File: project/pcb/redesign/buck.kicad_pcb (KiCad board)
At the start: 2 copper layers, 105.5 x 81 mm, 57 parts, among them J1 12V FUSED INPUT, J2 LOAD + / -, J3 NUCLEO-L432KC EXT USB, Q1 IRFZ44N TO-220, Q2 MMBT3904, U1 IR2110STRPBF, U2 78M05, U3 SN74HCT14DR, U4 SN74HCT00DR, U5 LM393BIDR, U6 INA180A1IDBVR

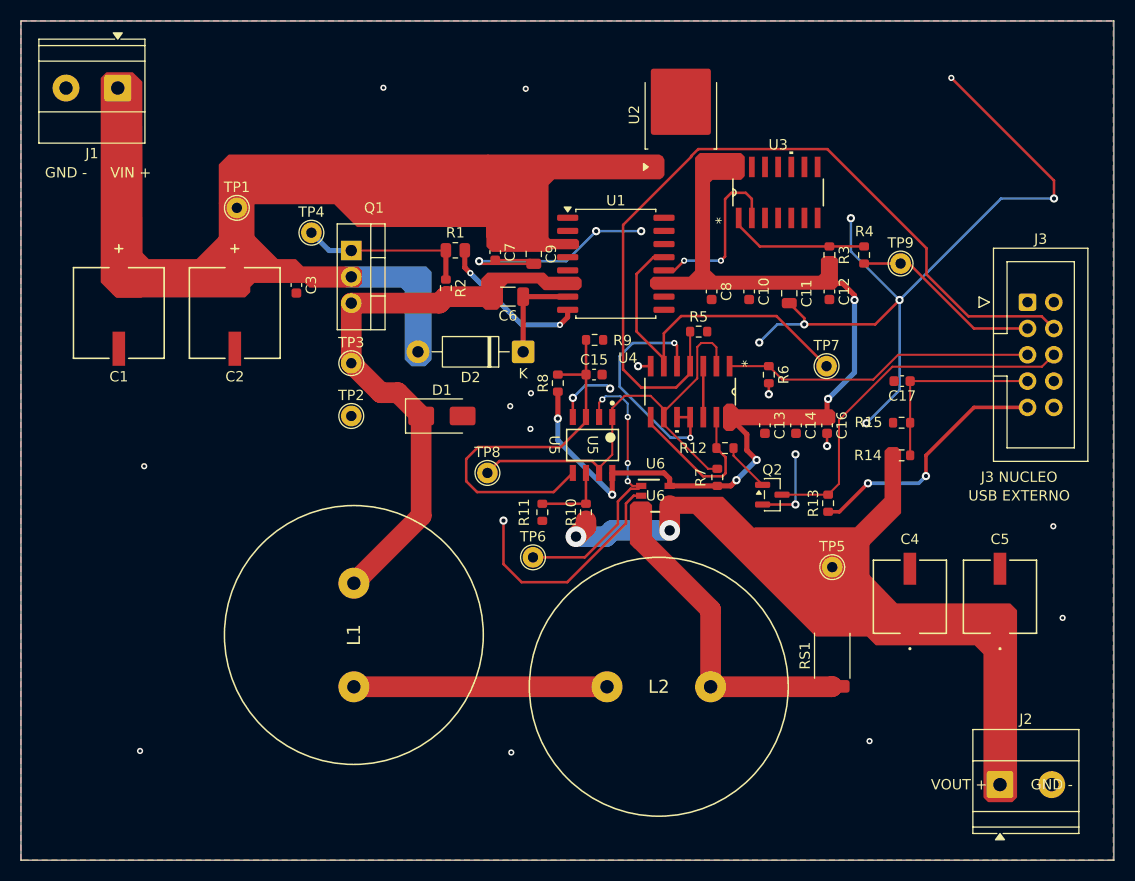
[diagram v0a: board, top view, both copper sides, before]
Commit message: feat: Buck PCB Rev B prototype package for JLCPCB
Rev B of project/pcb/redesign, prepared for a JLCPCB top-side SMT quote
and still pending bring-up. Rev A is preserved in history/revA_quote_20261027.

- Lands taken from manufacturer drawings (Murata 6000B, Same Sky TB002,
  Wurth WR-BHD, Panasonic SVPF/SVF, TA-I RLP, TI PW/DBV/DBZ/D/DBV5, Diodes
  SOD323); Q1 hole 1.4 mm per IPC-2222; U5 courtyard added.
- Power-domain interface: SN74LV4T125 buffer for PWM/RUN/RESET from +5V,
  TMUX1511 on the ADC path, TPS3808G33 supervisor, LM4040 2.5 V reference
  with BAT54WS clamps, fault latch set while the interface is disabled.
- Re-laid board: compact switching cell, no vias on HO/GATE/BOOT/SW,
  Kelvin sensing from RS1 inner edges, GND pours on both layers.
- L432KC firmware: Rev B ADC scale (6.4844 mV/count), VOUT-collapse fault,
  host test.
- Fabrication package production/jlcpcb-revB-2026-10-27: DRC 0 errors,
  0 unconnected, 0 parity; ERC 0 errors.

Not ready to order: L1/L2 have no JLC/LCSC stock, the LM4040 X-variant and
R10 supply need decisions, the JLC viewer rotation check and ARM build are
pending. BUCK_BOARD_REVIEWED stays 0. See revB_release_report.md.

Co-Authored-By: Claude Opus 5.5 <noreply@anthropic.com>
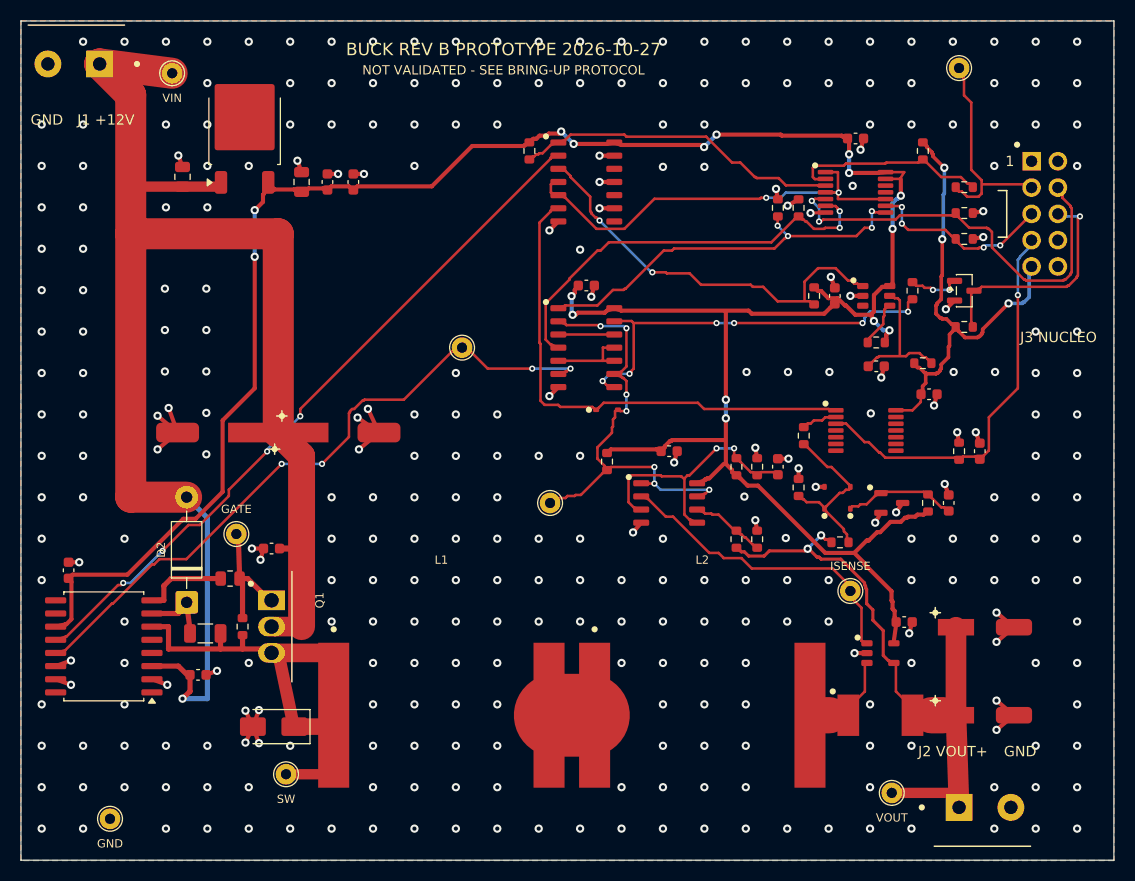
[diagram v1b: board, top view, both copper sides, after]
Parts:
- added C18: 100nF, Capacitor_SMD:C_0603_1608Metric, F.Cu at (186.0, 42.8)
- added C19: 100nF, Capacitor_SMD:C_0603_1608Metric, F.Cu at (193.1, 67.5)
- added C20: 100nF, Capacitor_SMD:C_0603_1608Metric, F.Cu at (184.0, 58.0)
- added C21: 1nF, Capacitor_SMD:C_0603_1608Metric, F.Cu at (188.0, 64.8)
- added C22: 100nF, Capacitor_SMD:C_0603_1608Metric, F.Cu at (195.0, 78.0)
- added D3: BAT54WS-7-F, Buck_RevB:Diodes_SOD323, F.Cu at (183.0, 77.5)
- added D4: BAT54WS-7-F, Buck_RevB:Diodes_SOD323, F.Cu at (185.5, 77.5)
- added D5: BAT54WS-7-F, Buck_RevB:Diodes_SOD323, F.Cu at (162.0, 69.0)
- added R16: 10k, Resistor_SMD:R_0603_1608Metric, F.Cu at (180.5, 49.5)
- added R17: 10k, Resistor_SMD:R_0603_1608Metric, F.Cu at (178.5, 49.5)
- added R18: 100k, Resistor_SMD:R_0603_1608Metric, F.Cu at (192.5, 44.0)
- added R19: 22k, Resistor_SMD:R_0603_1608Metric, F.Cu at (182.0, 58.0)
- added R20: 1k 1%, Resistor_SMD:R_0603_1608Metric, F.Cu at (181.0, 71.5)
- added R21: 100k 1%, Resistor_SMD:R_0603_1608Metric, F.Cu at (196.0, 73.0)
- added R22: 10k, Resistor_SMD:R_0603_1608Metric, F.Cu at (192.5, 64.5)
- added R23: 2.2k, Resistor_SMD:R_0603_1608Metric, F.Cu at (193.0, 78.0)
- added R24: 100k, Resistor_SMD:R_0603_1608Metric, F.Cu at (188.0, 62.5)
- added U10: LM4040AIM3X-2.5/NOPB, Buck_RevB:TI_DBZ0003A_SOT-23-3, F.Cu at (189.5, 78.0)
- added U7: SN74LV4T125PWR, Buck_RevB:TI_PW0014A_TSSOP-14, F.Cu at (186.0, 48.0)
- added U8: TMUX1511PWR, Buck_RevB:TI_PW0014A_TSSOP-14, F.Cu at (187.0, 71.0)
- added U9: TPS3808G33DBVR, Buck_RevB:TI_DBV0006A_SOT-23-6, F.Cu at (188.0, 58.0)
- C1, C2: footprint Buck_SMD:PCAP_SVP_E7_PAN -> Buck_RevB:CP_Panasonic_SVPF_E7_Land
- C4, C5: value 10uF 35V low ESR -> 10uF 50V 50SVF10M; footprint Buck_SMD:CAP_SVF_C6_PAN -> Buck_RevB:CP_Panasonic_SVF_C6_Land
- D2: value UF4004 -> UF4004-E3/54
- J1: value 12V FUSED INPUT -> 12V IN TB002-500-02BE; footprint TerminalBlock_Phoenix:TerminalBlock_Phoenix_MKDS-1,5-2_1x02_P5.00mm_Horizontal -> Buck_RevB:TerminalBlock_SameSky_TB002-500-02_1x02_P5.00mm
- J2: value LOAD + / - -> LOAD TB002-500-02BE; footprint TerminalBlock_Phoenix:TerminalBlock_Phoenix_MKDS-1,5-2_1x02_P5.00mm_Horizontal -> Buck_RevB:TerminalBlock_SameSky_TB002-500-02_1x02_P5.00mm
- J3: value NUCLEO-L432KC EXT USB -> NUCLEO IF 61201021621; footprint Connector_IDC:IDC-Header_2x05_P2.54mm_Vertical -> Buck_RevB:Wurth_WR-BHD_61201021621_2x05_P2.54mm_Vertical
- L1, L2: value 330uH >=3A Isat VERIFY -> 330uH 60B334C; footprint Buck:Inductor_25mm_P10mm_VERIFY -> Buck_RevB:L_Murata_6000B_27.0x23.5mm
- Q1: value IRFZ44N TO-220 -> IRFZ44NPBF; footprint Package_TO_SOT_THT:TO-220-3_Vertical -> Buck_RevB:TO-220-3_Vertical_Drill1.4
- RS1: value 0.050R 1% 1W -> 0.050R 1% 2W RLP25FEER050; footprint Resistor_SMD:R_2512_6332Metric -> Buck_RevB:R_TAI_RLP25_2512_Kelvin
- U3, U4: footprint Buck_SMD:D14 -> Buck_RevB:TI_D0014A_SOIC-14
- U5: footprint Buck_SMD:D0008A-MFG -> Buck_RevB:TI_D0008A_SOIC-8
- U6: footprint Buck_SMD:DBV0005A_N -> Buck_RevB:TI_DBV0005A_SOT-23-5
- moved C8 67.7 mm to (110.0, 84.5), turned to 90 degrees
- moved U1 61.7 mm to (113.4, 91.8), turned to 180 degrees
- moved C7 49.9 mm to (122.5, 94.6), turned to 0 degrees
- moved C11 48.3 mm to (132.5, 47.0), turned to 90 degrees
- moved C12 47.2 mm to (137.5, 47.0), turned to 90 degrees
- moved TP2 45.3 mm to (114.0, 108.5)
- moved C6 43.7 mm to (123.2, 90.6), turned to 0 degrees
- moved U2 42.2 mm to (127.0, 42.0)
- moved C10 42.1 mm to (135.0, 47.0), turned to 90 degrees
- moved D2 40.5 mm to (121.4, 87.6), turned to 90 degrees
- moved TP3 40.2 mm to (131.0, 104.2)
- moved R1 38.4 mm to (125.6, 85.3), turned to 0 degrees
- moved R2 38.1 mm to (126.8, 89.9)
- moved TP7 35.2 mm to (148.0, 63.0)
- moved C9 34.7 mm to (121.0, 46.5), turned to 90 degrees
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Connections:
- R14 pad 2: VSENSE -> VSENSE_DIV
- R15 pad 1: VSENSE -> VSENSE_DIV
- R4 pad 2: DPRIME -> PWM_IN
- U3 pad 3: GND -> NUC_PG
- U3 pad 4: unconnected-(U3-2Y-Pad4) -> BUF_OE_N
- U3 pad 5: GND -> BUF_OE_N
- U3 pad 6: unconnected-(U3-3Y-Pad6) -> ADC_EN
- U4 pad 1: RESET -> RESET_5V
- U4 pad 4: RUN -> RUN_5V
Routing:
- net +5V: track 53.1 -> 244.4 mm, vias 6 -> 16
- net VIN: track 0.00 -> 149.6 mm, vias 0 -> 1
- net GND: track 142.2 -> 79.9 mm, vias 29 -> 321
- net HIN: track 16.9 -> 68.7 mm, vias 2 -> 4
- net ADC_EN: track 0.00 -> 49.0 mm
- net RUN_5V: track 0.00 -> 40.7 mm, vias 0 -> 2
- net BUF_OE_N: track 0.00 -> 40.5 mm, vias 0 -> 2
- net VOUT: track 13.6 -> 53.8 mm
- net NUC_PG: track 0.00 -> 39.6 mm, vias 0 -> 2
- net RESET_5V: track 0.00 -> 38.4 mm, vias 0 -> 4
- net RUN: track 79.1 -> 41.1 mm, vias 0 -> 2
- net SD: track 34.9 -> 65.3 mm, vias 0 -> 4
- net IP: track 28.7 -> 4.53 mm
- net FAULT: track 15.9 -> 39.7 mm, vias 0 -> 6
- net LMID: track 24.4 -> 3.20 mm
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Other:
- board text added: "1"
- board text added: "BUCK REV B PROTOTYPE 2026-10-27"
- board text added: "GATE"
- board text added: "GND"
- board text added: "ISENSE"
- board text added: "J1 +12V"
- board text added: "J2 VOUT+"
- board text added: "NOT VALIDATED - SEE BRING-UP PROTOCOL"
- board text added: "SW"
- board text added: "VIN"
- board text added: "VOUT"
- board text removed: "GND -"
- board text removed: "USB EXTERNO"
- board text removed: "VIN +"
- board text removed: "VOUT +"

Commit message: fix: make Buck Rev B orderable as a lab prototype
Order decisions after an external second opinion:
- Move the L1-L2-RS1-output chain 2 mm right: Q1 tab (VIN) to L1 SW clip
  clearance 1.28 -> 3.29 mm at maximum package dimensions; board rerouted,
  DRC 0 errors / 0 unconnected / 0 parity.
- L1/L2 (60B334C, no JLC/LCSC stock) leave the JLC BOM/CPL and are
  hand-soldered: 31 BOM lines, 62 placements, all with JLC stock.
- R10 -> UNI-ROYAL 0603WAF3092T5E (C23022), same 30.9k 1% 0603.
- Accept LM4040AIM3X-2.5/NOPB (same device per TI SNOS633N s.11).
- Document lab-only use: regulated 12 V, resistive load, supervised tests.

Co-Authored-By: Claude Opus 5.5 <noreply@anthropic.com>
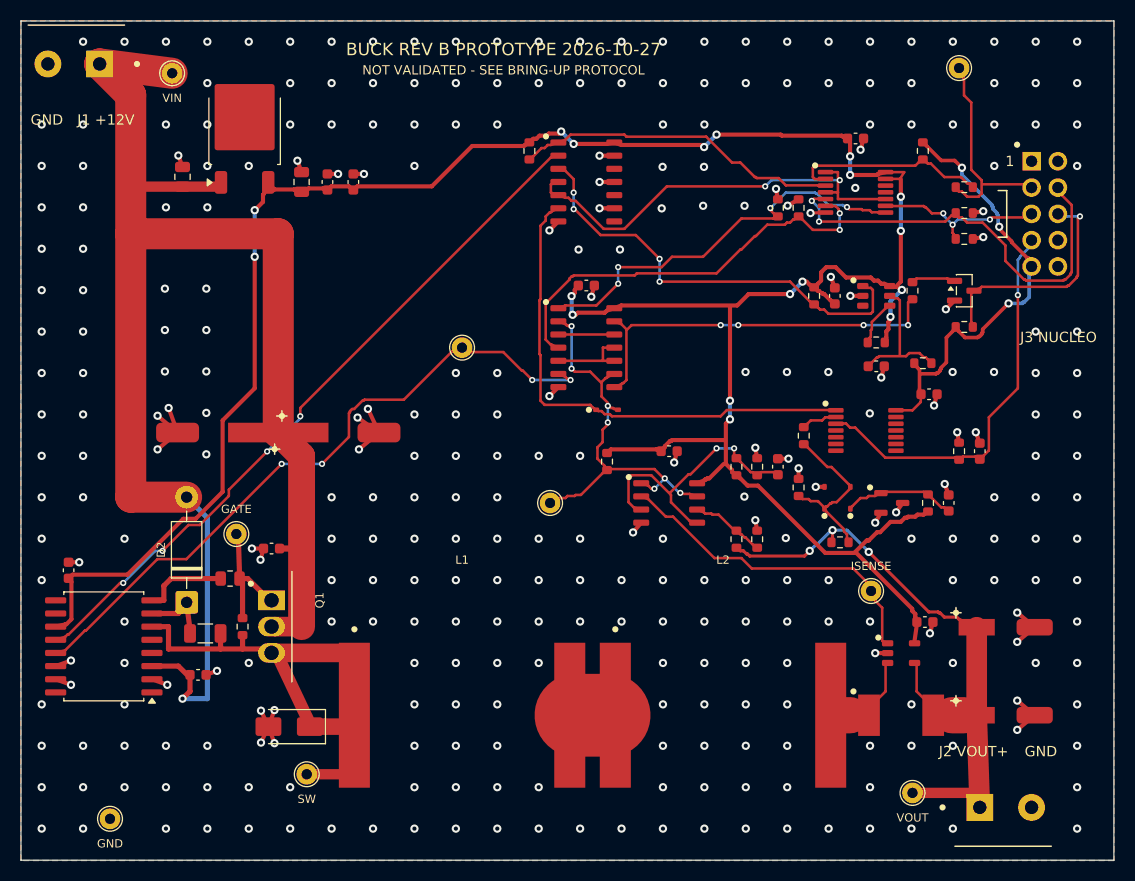
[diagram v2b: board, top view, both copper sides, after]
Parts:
- moved C16 2.00 mm to (192.7, 89.5)
- moved C4 2.00 mm to (200.5, 98.5)
- moved C5 2.00 mm to (200.5, 90.0)
- moved J2 2.00 mm to (198.0, 107.4)
- moved L1 2.00 mm to (148.0, 98.5)
- moved L2 2.00 mm to (173.2, 98.5)
- moved RS1 2.00 mm to (190.4, 98.5)
- moved TP3 2.00 mm to (133.0, 104.2)
- moved TP5 2.00 mm to (191.5, 106.0)
- moved TP6 2.00 mm to (187.5, 86.5)
- moved U6 2.00 mm to (190.4, 92.5)
- moved D1 1.50 mm to (131.3, 99.6)
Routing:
- net NTRIP: track 45.0 -> 39.7 mm
- net +5V: track 244.4 -> 249.0 mm, vias 16 -> 18
- net VOUT: track 53.8 -> 56.8 mm, vias 2 -> 3
- net SW: track 32.2 -> 35.2 mm
- net NUC_3V3: track 45.5 -> 42.5 mm
- net NUC_PG: track 39.6 -> 42.3 mm, vias 2 -> 4
- net FAULT: track 39.7 -> 37.7 mm, vias 6 -> 4
- net ISENSE: track 29.9 -> 31.9 mm
- net RESET: track 18.1 -> 16.5 mm, vias 4 -> 3
- net RESET_5V: track 38.4 -> 39.4 mm
- net FB: track 5.04 -> 4.24 mm, vias 2 -> 0
- net BUF_OE_N: track 40.5 -> 41.2 mm
- net GND: vias 321 -> 323

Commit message: feat: replace Buck Rev B L1+L2 with a single JLC-placed 60B684C
L1+L2 (2 x Murata 60B334C in series) have no JLCPCB/LCSC stock, which
forced buying them at DigiKey and hand-soldering. A single Murata
60B684C (680 uH, 3 A, 135 mOhm, C6095796, JLC stock 17) from the same
6000B series uses the same drawing and land, so JLCPCB can place it.

- Schematic: L1 becomes 60B684C, L2 and the LMID net are removed and
  L1.2 joins IP (revb_tools/sch_single_inductor.py). ERC 0 errors;
  netdiff shows only those three changes.
- PCB: L2 removed, 3.5 mm F.Cu track from L1 pad 2 to the outer end of
  RS1; Kelvin traces and the 3.285 mm Q1 tab to L1 gap are unchanged.
  DRC 0 errors / 0 unconnected / 0 parity, same 3 justified width
  warnings. Stale LMID references removed from the SW width rule and
  netclass patterns.
- Package: BOM 32 lines / CPL 63 placements, all lines in JLC stock,
  manual list now only J1, J2, J3, Q1, D2. Hashes regenerated.
- Docs: +3 % inductance vs the 660 uH assignment value, losses, ripple,
  first power-on L1 check (578-782 uH, <= 135 mOhm) and the portal
  check that JLC accepts the 37 g / 20 mm part.

BUCK_BOARD_REVIEWED stays 0; firmware unchanged.

Co-Authored-By: Claude Opus 5.5 <noreply@anthropic.com>
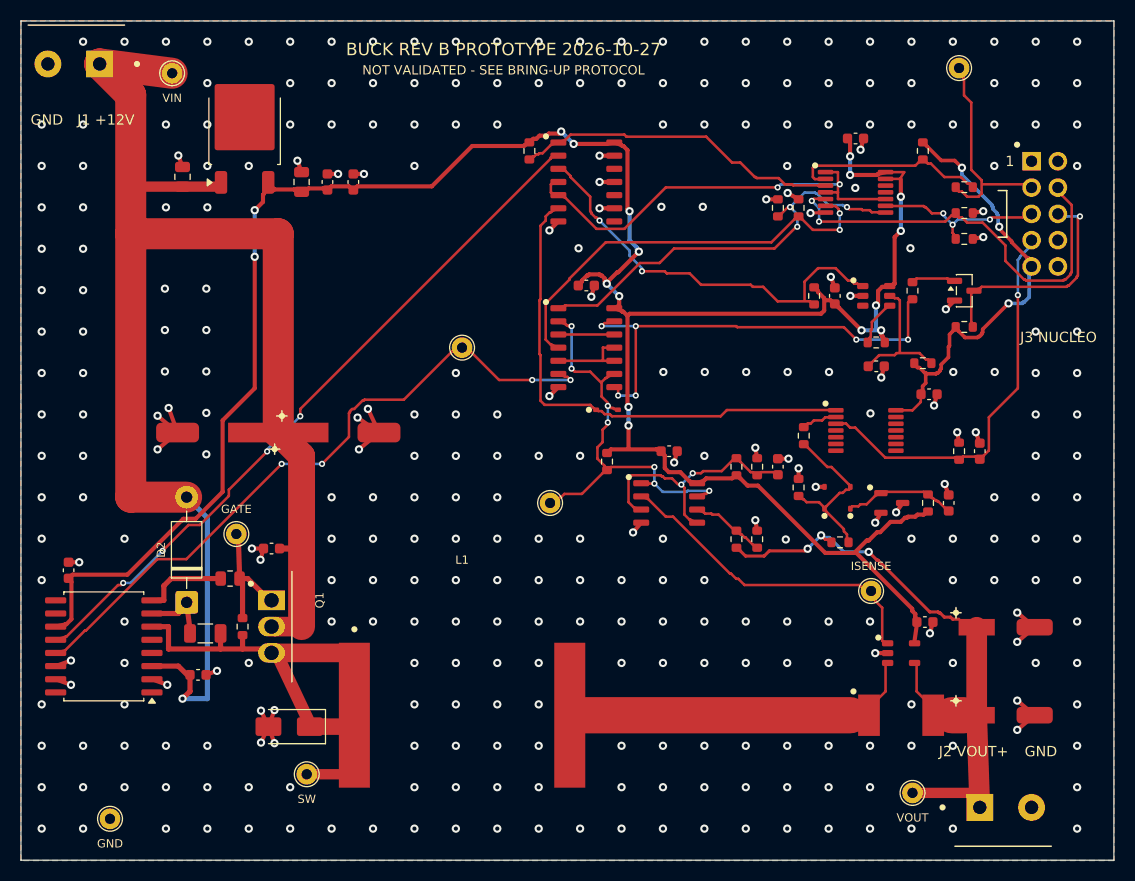
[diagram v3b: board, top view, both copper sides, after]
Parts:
- removed L2: 330uH 60B334C, Buck_RevB:L_Murata_6000B_27.0x23.5mm
- L1: value 330uH 60B334C -> 680uH 60B684C
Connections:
- L1 pad 2: LMID -> IP
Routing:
- net IP: track 4.53 -> 30.2 mm
- net +5V: track 249.0 -> 233.8 mm, vias 18 -> 17
- net FAULT: track 37.7 -> 44.9 mm, vias 4 -> 6
- net LMID: track 3.20 -> 0.00 mm
- net NUC_PG: track 42.3 -> 40.1 mm, vias 4 -> 2
- net VOUT: track 56.8 -> 54.6 mm
- net NTRIP: track 39.7 -> 41.7 mm
- net VREF: track 26.6 -> 24.7 mm
- net RESET_5V: track 39.4 -> 40.3 mm, vias 4 -> 3
- net GND: track 79.9 -> 80.0 mm, vias 323 -> 326
